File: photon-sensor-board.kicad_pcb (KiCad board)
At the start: 2 copper layers, 35 x 50 mm, 6 parts, among them U1 PHOTON, U2 DS18B20

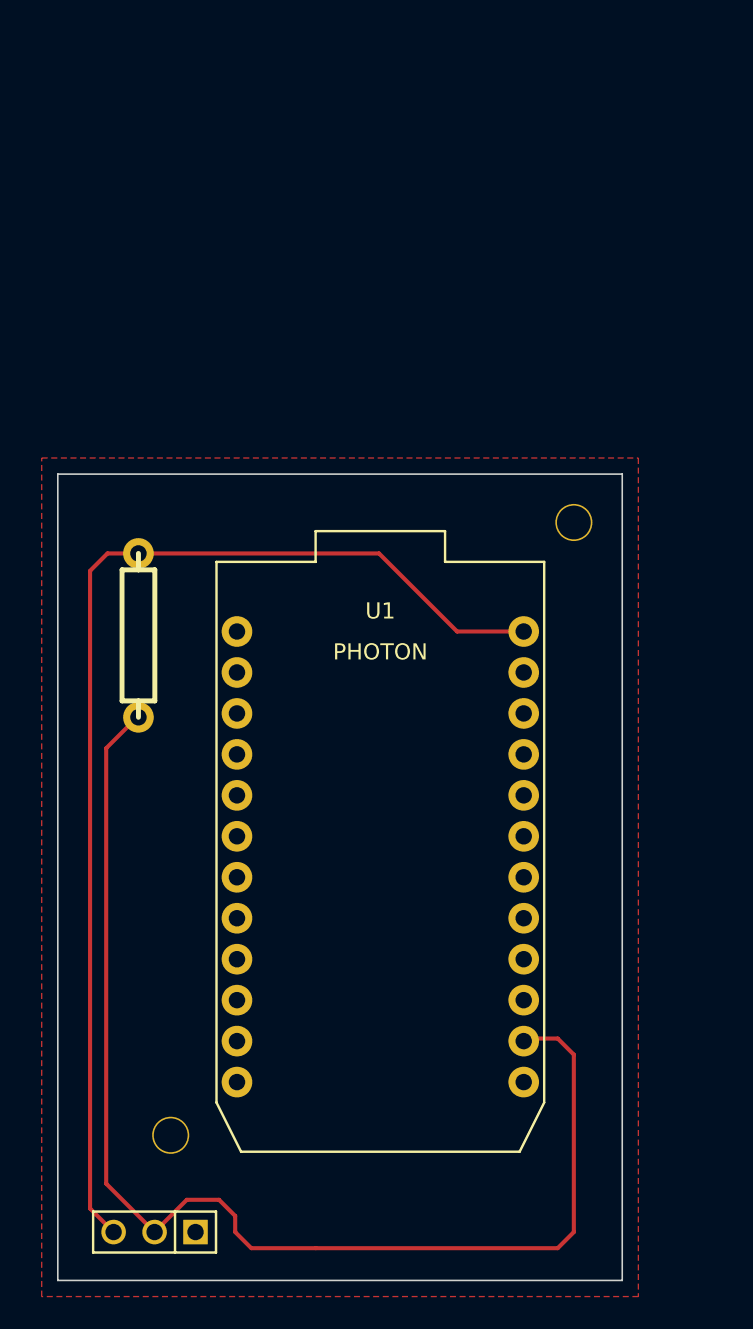
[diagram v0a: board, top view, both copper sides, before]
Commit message: Updated some footprints with new libraries
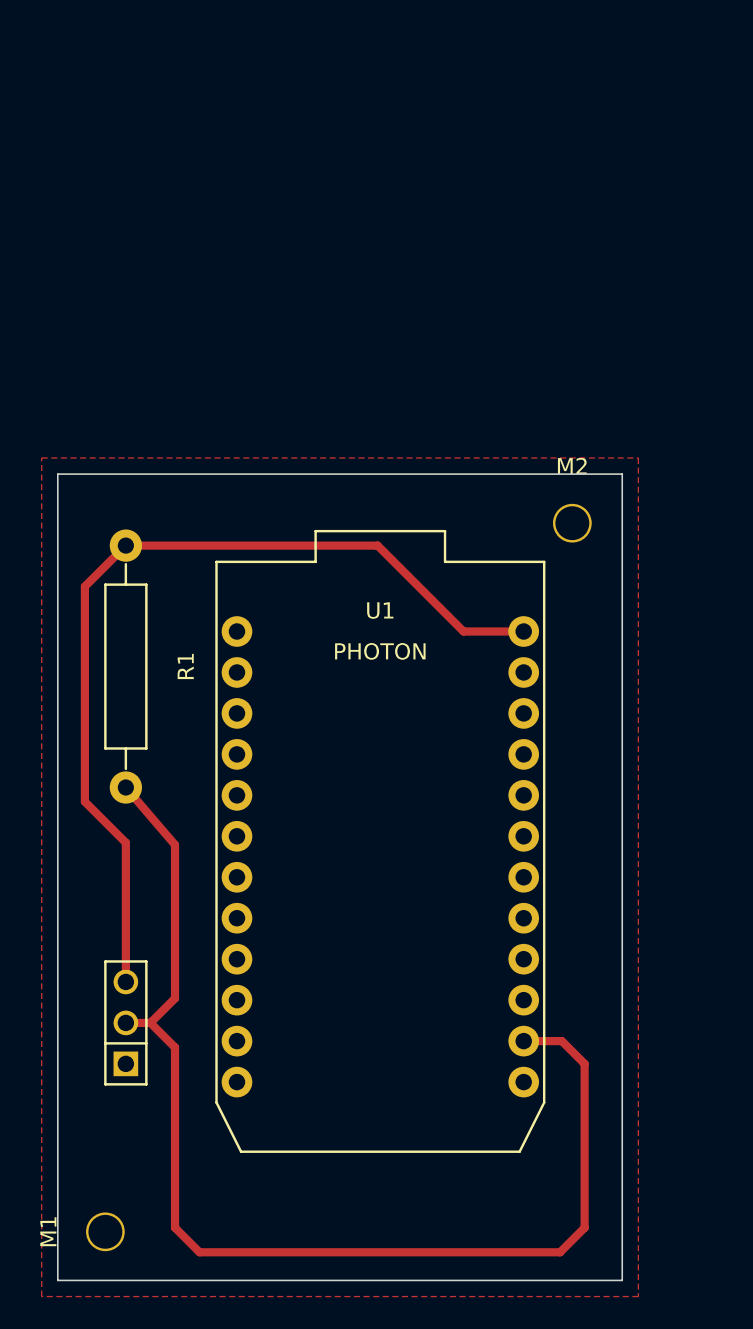
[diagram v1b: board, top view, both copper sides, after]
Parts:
- removed 1PIN (x2): P***, 1pin
- added M1: MountingHole_2-5mm, Mounting_Holes:MountingHole_2-5mm, F.Cu at (108.0, 142.0)
- added M2: MountingHole_2-5mm, Mounting_Holes:MountingHole_2-5mm, F.Cu at (136.9, 98.0)
- R1: footprint R4 -> Resistors_ThroughHole:Resistor_Horizontal_RM15mm
- U1: footprint PHOTON -> particle:photon
- moved U2 13.1 mm to (109.2, 129.0), turned to 90 degrees
- moved R1 2.09 mm to (109.2, 106.9)
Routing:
- net Net-(R1-Pad1): track 70.9 -> 56.0 mm
- net Net-(R1-Pad2): track 77.7 -> 72.6 mm
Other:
- net class Default: clearance 0.254 -> 0.381; trace_width 0.254 -> 0.508
- rule trace_clearance: 0.254 -> 0.381
- rule trace_min: 0.254 -> 0.508
- board text removed: "Photon Sensor Board v1.0 2015"

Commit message: Some adjustments
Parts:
- moved U2 26.4 mm to (114.3, 103.1)
- moved G*** 26.4 mm to (130.1, 88.1)
- moved R1 26.4 mm to (114.3, 81.0)
- moved U1 26.4 mm to (130.1, 94.1)
- moved M2 26.4 mm to (142.0, 72.1)
- moved M1 26.4 mm to (113.0, 116.1)
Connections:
- U1 pad 13: Net-(U1-Pad13) -> Net-(R1-Pad2)
- U1 pad 14: Net-(R1-Pad2) -> Net-(U1-Pad14)
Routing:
- net Net-(R1-Pad2): track 72.6 -> 70.0 mm
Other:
- board text added: "Photon Sensor Board v1.1 2015"
